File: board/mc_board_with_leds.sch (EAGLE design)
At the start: 30 parts, among them IC2 MEGA8-P, Q2 16MHz

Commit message: renamed LEDs in .c file and schematic
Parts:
- removed LED1, LED2, LED3, LED4, LED5, LED6, LED7, LED8: (no value), led:LED3MM
- added LED_STRICH_1, LED_STRICH_2, LED_STRICH_3, LED_STRICH_4, LED_ZAUN_1, LED_ZAUN_2, LED_ZAUN_3, LED_ZAUN_4: (no value), led:LED3MM
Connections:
- net PB0/LED4 renamed PB0/LED_STRICH_4
- net PC4/LED6 renamed PC4/LED_ZAUN_2
- net PC5/LED5 renamed PC5/LED_ZAUN_1
- net PD3/LED7 renamed PD3/LED_ZAUN_3
- net PD4/LED8 renamed PD4/LED_ZAUN_4
- net PD5/LED1 renamed PD5/LED_STRICH_1
- net PD6/LED2 renamed PD6/LED_STRICH_2
- net PD7/LED3 renamed PD7/LED_STRICH_3
- net GND: now also LED_STRICH_1.C, LED_STRICH_2.C, LED_STRICH_3.C, LED_STRICH_4.C, LED_ZAUN_1.C, LED_ZAUN_2.C, LED_ZAUN_3.C, LED_ZAUN_4.C; no longer LED1.C, LED2.C, LED3.C, LED4.C, LED5.C, LED6.C, LED7.C, LED8.C
- net N$1: now also LED_STRICH_1.A; no longer LED1.A
- net N$10: now also LED_ZAUN_2.A; no longer LED6.A
- net N$11: now also LED_ZAUN_3.A; no longer LED7.A
- net N$12: now also LED_ZAUN_4.A; no longer LED8.A
- net N$2: now also LED_STRICH_2.A; no longer LED2.A
- net N$3: now also LED_STRICH_3.A; no longer LED3.A
- net N$7: now also LED_STRICH_4.A; no longer LED4.A
- net N$8: now also LED_ZAUN_1.A; no longer LED5.A
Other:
- moved on the sheet: C7, PWRLED, R1, R10, R11, R3, R4, R6, R7, R8, R9, S2

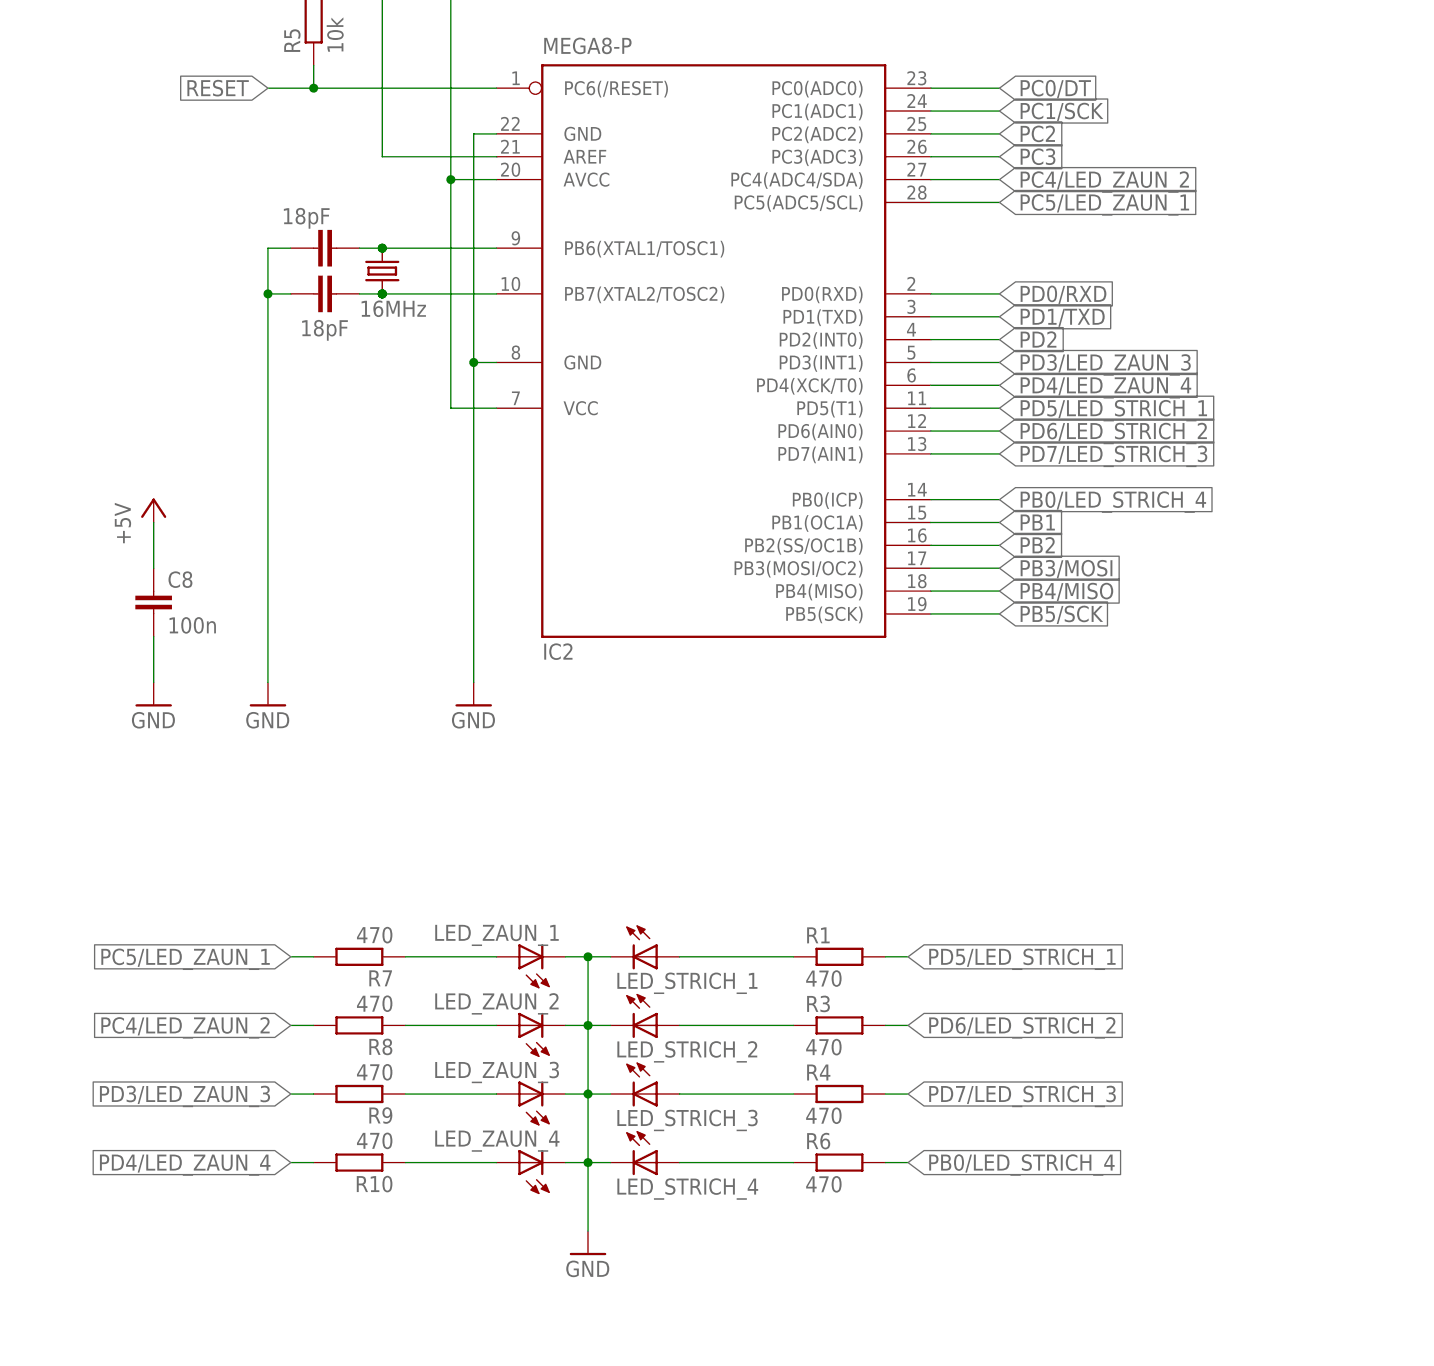
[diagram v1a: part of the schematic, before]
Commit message: reordered leds
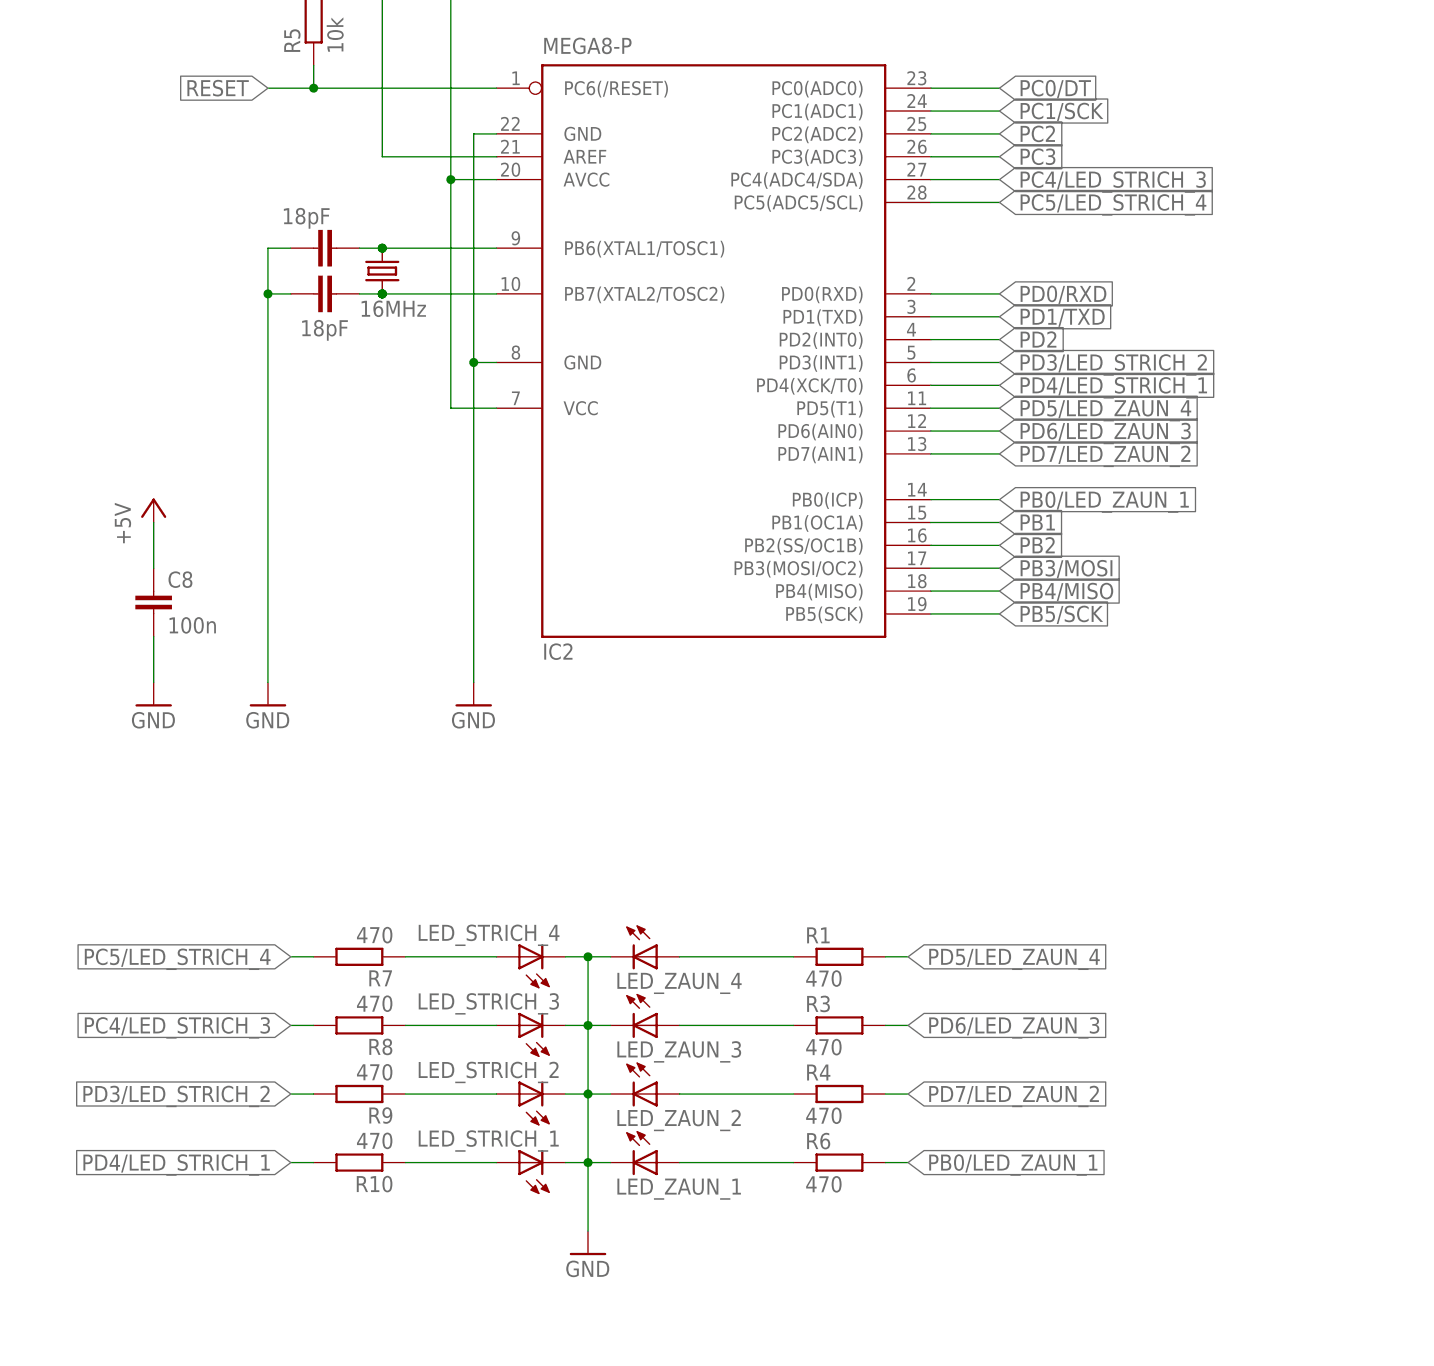
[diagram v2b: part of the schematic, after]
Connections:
- net PB0/LED_STRICH_4 renamed PB0/LED_ZAUN_1
- net PC4/LED_ZAUN_2 renamed PC4/LED_STRICH_3
- net PC5/LED_ZAUN_1 renamed PC5/LED_STRICH_4
- net PD3/LED_ZAUN_3 renamed PD3/LED_STRICH_2
- net PD4/LED_ZAUN_4 renamed PD4/LED_STRICH_1
- net PD5/LED_STRICH_1 renamed PD5/LED_ZAUN_4
- net PD6/LED_STRICH_2 renamed PD6/LED_ZAUN_3
- net PD7/LED_STRICH_3 renamed PD7/LED_ZAUN_2
- net N$1: now also LED_ZAUN_4.A; no longer LED_STRICH_1.A
- net N$10: now also LED_STRICH_3.A; no longer LED_ZAUN_2.A
- net N$11: now also LED_STRICH_2.A; no longer LED_ZAUN_3.A
- net N$12: now also LED_STRICH_1.A; no longer LED_ZAUN_4.A
- net N$2: now also LED_ZAUN_3.A; no longer LED_STRICH_2.A
- net N$3: now also LED_ZAUN_2.A; no longer LED_STRICH_3.A
- net N$7: now also LED_ZAUN_1.A; no longer LED_STRICH_4.A
- net N$8: now also LED_STRICH_4.A; no longer LED_ZAUN_1.A
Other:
- moved on the sheet: LED_STRICH_1, LED_STRICH_2, LED_STRICH_3, LED_STRICH_4, LED_ZAUN_1, LED_ZAUN_2, LED_ZAUN_3, LED_ZAUN_4
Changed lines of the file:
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@@
 <part name="R4" library="resistor" deviceset="R-EU_" device="R0805" value="470"/>
 <part name="R6" library="resistor" deviceset="R-EU_" device="R0805" value="470"/>
-<part name="LED_STRICH_1" library="led" deviceset="LED" device="3MM"/>
-<part name="LED_STRICH_2" library="led" deviceset="LED" device="3MM"/>
-<part name="LED_STRICH_3" library="led" deviceset="LED" device="3MM"/>
-<part name="LED_STRICH_4" library="led" deviceset="LED" device="3MM"/>
+<part name="LED_ZAUN_4" library="led" deviceset="LED" device="3MM"/>
+<part name="LED_ZAUN_3" library="led" deviceset="LED" device="3MM"/>
+<part name="LED_ZAUN_2" library="led" deviceset="LED" device="3MM"/>
+<part name="LED_ZAUN_1" library="led" deviceset="LED" device="3MM"/>
 <part name="GND8" library="supply1" deviceset="GND" device=""/>
 <part name="R7" library="resistor" deviceset="R-EU_" device="R0805" value="470"/>
@@
 <part name="R9" library="resistor" deviceset="R-EU_" device="R0805" value="470"/>
 <part name="R10" library="resistor" deviceset="R-EU_" device="R0805" value="470"/>
-<part name="LED_ZAUN_1" library="led" deviceset="LED" device="3MM"/>
-<part name="LED_ZAUN_2" library="led" deviceset="LED" device="3MM"/>
-<part name="LED_ZAUN_3" library="led" deviceset="LED" device="3MM"/>
-<part name="LED_ZAUN_4" library="led" deviceset="LED" device="3MM"/>
+<part name="LED_STRICH_4" library="led" deviceset="LED" device="3MM"/>
+<part name="LED_STRICH_3" library="led" deviceset="LED" device="3MM"/>
+<part name="LED_STRICH_2" library="led" deviceset="LED" device="3MM"/>
+<part name="LED_STRICH_1" library="led" deviceset="LED" device="3MM"/>
 <part name="GND12" library="supply1" deviceset="GND" device=""/>
 <part name="R11" library="resistor" deviceset="R-EU_" device="R0805" value="470"/>
@@
 <instance part="R4" gate="G$1" x="205.74" y="-2.54"/>
 <instance part="R6" gate="G$1" x="205.74" y="-10.16"/>
-<instance part="LED_STRICH_1" gate="G$1" x="185.42" y="12.7" rot="R270"/>
-<instance part="LED_STRICH_2" gate="G$1" x="185.42" y="5.08" rot="R270"/>
-<instance part="LED_STRICH_3" gate="G$1" x="185.42" y="-2.54" rot="R270"/>
-<instance part="LED_STRICH_4" gate="G$1" x="185.42" y="-10.16" rot="R270"/>
+<instance part="LED_ZAUN_4" gate="G$1" x="185.42" y="12.7" rot="R270"/>
+<instance part="LED_ZAUN_3" gate="G$1" x="185.42" y="5.08" rot="R270"/>
+<instance part="LED_ZAUN_2" gate="G$1" x="185.42" y="-2.54" rot="R270"/>
+<instance part="LED_ZAUN_1" gate="G$1" x="185.42" y="-10.16" rot="R270"/>
 <instance part="GND8" gate="1" x="177.8" y="-20.32"/>
 <instance part="R7" gate="G$1" x="152.4" y="12.7" rot="R180"/>
@@
 <instance part="R9" gate="G$1" x="152.4" y="-2.54" rot="R180"/>
 <instance part="R10" gate="G$1" x="152.4" y="-10.16" rot="R180"/>
-<instance part="LED_ZAUN_1" gate="G$1" x="170.18" y="12.7" rot="R90"/>
-<instance part="LED_ZAUN_2" gate="G$1" x="170.18" y="5.08" rot="R90"/>
-<instance part="LED_ZAUN_3" gate="G$1" x="170.18" y="-2.54" rot="R90"/>
-<instance part="LED_ZAUN_4" gate="G$1" x="170.18" y="-10.16" rot="R90"/>
+<instance part="LED_STRICH_4" gate="G$1" x="170.18" y="12.7" rot="R90"/>
+<instance part="LED_STRICH_3" gate="G$1" x="170.18" y="5.08" rot="R90"/>
+<instance part="LED_STRICH_2" gate="G$1" x="170.18" y="-2.54" rot="R90"/>
+<instance part="LED_STRICH_1" gate="G$1" x="170.18" y="-10.16" rot="R90"/>
 <instance part="GND12" gate="1" x="177.8" y="-48.26"/>
 <instance part="R11" gate="G$1" x="160.02" y="-38.1" rot="R180"/>
@@
 <pinref part="R1" gate="G$1" pin="1"/>
 <wire x1="187.96" y1="12.7" x2="200.66" y2="12.7" width="0.1524" layer="91"/>
-<pinref part="LED_STRICH_1" gate="G$1" pin="A"/>
+<pinref part="LED_ZAUN_4" gate="G$1" pin="A"/>
 </segment>
 </net>
@@
 <pinref part="R3" gate="G$1" pin="1"/>
 <wire x1="187.96" y1="5.08" x2="200.66" y2="5.08" width="0.1524" layer="91"/>
-<pinref part="LED_STRICH_2" gate="G$1" pin="A"/>
+<pinref part="LED_ZAUN_3" gate="G$1" pin="A"/>
 </segment>
 </net>
@@
 <pinref part="R4" gate="G$1" pin="1"/>
 <wire x1="187.96" y1="-2.54" x2="200.66" y2="-2.54" width="0.1524" layer="91"/>
-<pinref part="LED_STRICH_3" gate="G$1" pin="A"/>
+<pinref part="LED_ZAUN_2" gate="G$1" pin="A"/>
 </segment>
 </net>
@@
 <pinref part="R6" gate="G$1" pin="1"/>
 <wire x1="187.96" y1="-10.16" x2="200.66" y2="-10.16" width="0.1524" layer="91"/>
-<pinref part="LED_STRICH_4" gate="G$1" pin="A"/>
+<pinref part="LED_ZAUN_1" gate="G$1" pin="A"/>
 </segment>
 </net>
@@
 <wire x1="177.8" y1="-2.54" x2="177.8" y2="-10.16" width="0.1524" layer="91"/>
 <wire x1="177.8" y1="-10.16" x2="180.34" y2="-10.16" width="0.1524" layer="91"/>
-<pinref part="LED_STRICH_1" gate="G$1" pin="C"/>
-<pinref part="LED_STRICH_2" gate="G$1" pin="C"/>
-<pinref part="LED_STRICH_3" gate="G$1" pin="C"/>
-<pinref part="LED_STRICH_4" gate="G$1" pin="C"/>
+<pinref part="LED_ZAUN_4" gate="G$1" pin="C"/>
+<pinref part="LED_ZAUN_3" gate="G$1" pin="C"/>
+<pinref part="LED_ZAUN_2" gate="G$1" pin="C"/>
+<pinref part="LED_ZAUN_1" gate="G$1" pin="C"/>
 <wire x1="177.8" y1="-10.16" x2="177.8" y2="-17.78" width="0.1524" layer="91"/>
 <pinref part="GND8" gate="1" pin="GND"/>
-<pinref part="LED_ZAUN_1" gate="G$1" pin="C"/>
+<pinref part="LED_STRICH_4" gate="G$1" pin="C"/>
 <wire x1="175.26" y1="12.7" x2="177.8" y2="12.7" width="0.1524" layer="91"/>
-<pinref part="LED_ZAUN_2" gate="G$1" pin="C"/>
+<pinref part="LED_STRICH_3" gate="G$1" pin="C"/>
 <wire x1="175.26" y1="5.08" x2="177.8" y2="5.08" width="0.1524" layer="91"/>
-<pinref part="LED_ZAUN_3" gate="G$1" pin="C"/>
+<pinref part="LED_STRICH_2" gate="G$1" pin="C"/>
 <wire x1="175.26" y1="-2.54" x2="177.8" y2="-2.54" width="0.1524" layer="91"/>
-<pinref part="LED_ZAUN_4" gate="G$1" pin="C"/>
+<pinref part="LED_STRICH_1" gate="G$1" pin="C"/>
 <wire x1="175.26" y1="-10.16" x2="177.8" y2="-10.16" width="0.1524" layer="91"/>
 <junction x="177.8" y="12.7"/>
@@
 <pinref part="R7" gate="G$1" pin="1"/>
 <wire x1="167.64" y1="12.7" x2="157.48" y2="12.7" width="0.1524" layer="91"/>
-<pinref part="LED_ZAUN_1" gate="G$1" pin="A"/>
+<pinref part="LED_STRICH_4" gate="G$1" pin="A"/>
 </segment>
 </net>
@@
 <pinref part="R8" gate="G$1" pin="1"/>
 <wire x1="167.64" y1="5.08" x2="157.48" y2="5.08" width="0.1524" layer="91"/>
-<pinref part="LED_ZAUN_2" gate="G$1" pin="A"/>
+<pinref part="LED_STRICH_3" gate="G$1" pin="A"/>
 </segment>
 </net>
@@
 <pinref part="R9" gate="G$1" pin="1"/>
 <wire x1="167.64" y1="-2.54" x2="157.48" y2="-2.54" width="0.1524" layer="91"/>
-<pinref part="LED_ZAUN_3" gate="G$1" pin="A"/>
+<pinref part="LED_STRICH_2" gate="G$1" pin="A"/>
 </segment>
 </net>
@@
 <pinref part="R10" gate="G$1" pin="1"/>
 <wire x1="167.64" y1="-10.16" x2="157.48" y2="-10.16" width="0.1524" layer="91"/>
-<pinref part="LED_ZAUN_4" gate="G$1" pin="A"/>
+<pinref part="LED_STRICH_1" gate="G$1" pin="A"/>
 </segment>
 </net>
@@
 </segment>
 </net>
-<net name="PD3/LED_ZAUN_3" class="0">
+<net name="PD3/LED_STRICH_2" class="0">
 <segment>
 <wire x1="215.9" y1="78.74" x2="223.52" y2="78.74" width="0.1524" layer="91"/>
@@
 </segment>
 </net>
-<net name="PD4/LED_ZAUN_4" class="0">
+<net name="PD4/LED_STRICH_1" class="0">
 <segment>
 <wire x1="223.52" y1="76.2" x2="215.9" y2="76.2" width="0.1524" layer="91"/>
@@
 </segment>
 </net>
-<net name="PC5/LED_ZAUN_1" class="0">
+<net name="PC5/LED_STRICH_4" class="0">
 <segment>
 <wire x1="215.9" y1="96.52" x2="223.52" y2="96.52" width="0.1524" layer="91"/>
@@
 </segment>
 </net>
-<net name="PC4/LED_ZAUN_2" class="0">
+<net name="PC4/LED_STRICH_3" class="0">
 <segment>
 <wire x1="215.9" y1="99.06" x2="223.52" y2="99.06" width="0.1524" layer="91"/>
@@
 </segment>
 </net>
-<net name="PB0/LED_STRICH_4" class="0">
+<net name="PB0/LED_ZAUN_1" class="0">
 <segment>
 <wire x1="223.52" y1="63.5" x2="215.9" y2="63.5" width="0.1524" layer="91"/>
@@
 </segment>
 </net>
-<net name="PD5/LED_STRICH_1" class="0">
+<net name="PD5/LED_ZAUN_4" class="0">
 <segment>
 <pinref part="R1" gate="G$1" pin="2"/>
@@
 </segment>
 </net>
-<net name="PD6/LED_STRICH_2" class="0">
+<net name="PD6/LED_ZAUN_3" class="0">
 <segment>
 <pinref part="R3" gate="G$1" pin="2"/>
@@
 </segment>
 </net>
-<net name="PD7/LED_STRICH_3" class="0">
+<net name="PD7/LED_ZAUN_2" class="0">
 <segment>
 <pinref part="R4" gate="G$1" pin="2"/>
